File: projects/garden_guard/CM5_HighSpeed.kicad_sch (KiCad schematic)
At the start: 28 parts, among them J1 Conn_02x07_Odd_Even, J2 Conn_01x03, J3 Conn_01x04, J4 Micro_SD_Card_Det, SW1 Tact button, U1 SN74LVC1G07DBVR, U2 TPD4EUSB30, U3 TPD4EUSB30, U4 RT9742GGJ5, U5 MagJack-A70-112-331N126

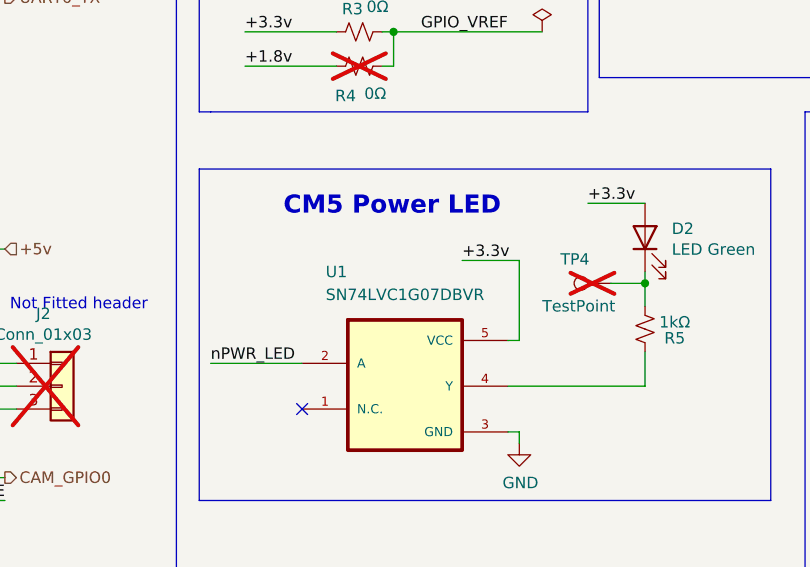
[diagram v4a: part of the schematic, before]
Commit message: - Assign 3D models to lingering footprints lacking them - Start playing with board layout - Move CM5 library files from project to components dir
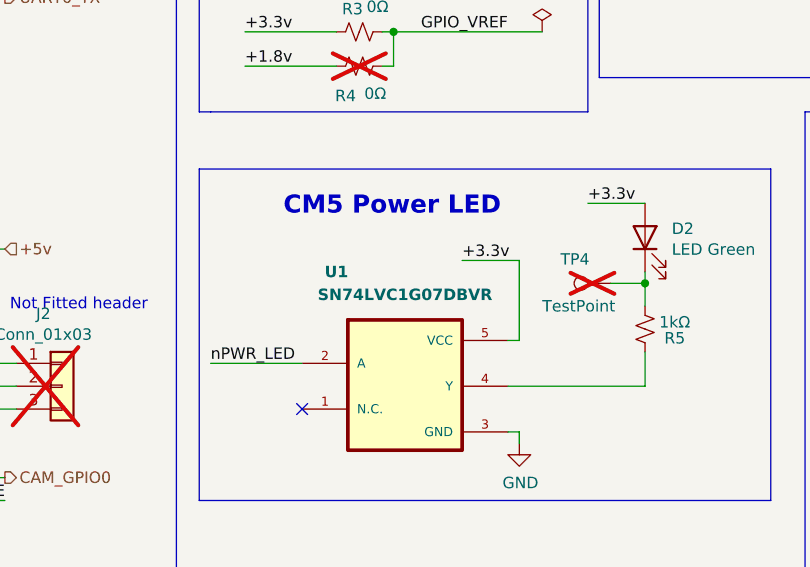
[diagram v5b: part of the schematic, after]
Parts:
- Module1: footprint CM5IO:Raspberry-Pi-5-Compute-Module -> CM5IO:Raspberry-Pi-5-Compute-Module_tall
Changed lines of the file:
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@@
 				(font
 					(size 1.27 1.27)
+					(thickness 0.254)
+					(bold yes)
 				)
 			)
@@
 				(font
 					(size 1.27 1.27)
+					(thickness 0.254)
+					(bold yes)
 				)
 			)
@@
 			)
 		)
-		(property "Footprint" "CM5IO:Raspberry-Pi-5-Compute-Module"
+		(property "Footprint" "CM5IO:Raspberry-Pi-5-Compute-Module_tall"
 			(at 214.63 104.14 0)
 			(effects

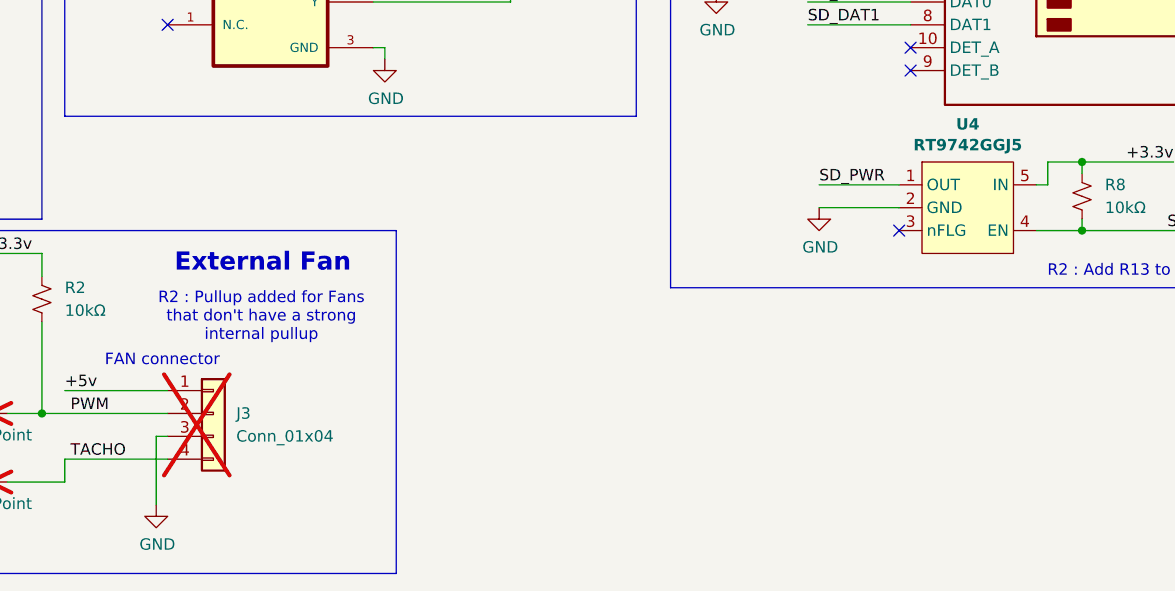
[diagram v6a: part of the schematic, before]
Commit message: - Add M.2 power and connector layout - Add micro HDMI to schematic and layout - Add microSD layout - Add IR illuminator and solenoid output MOSFET layouts - Add USB-C layout
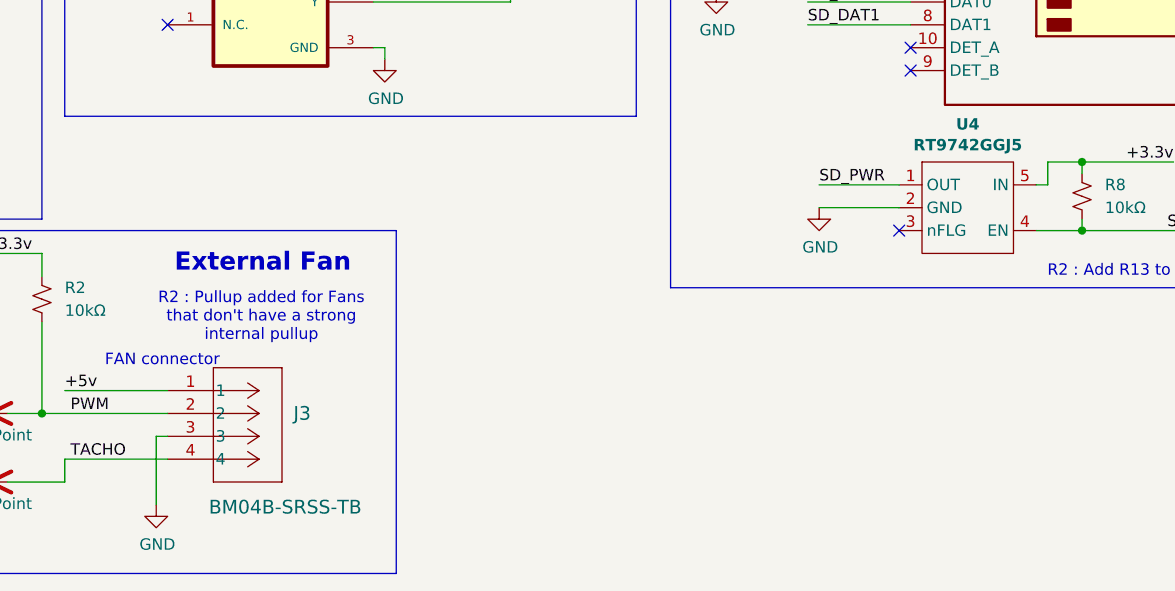
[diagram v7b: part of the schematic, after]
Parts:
- removed J3: Conn_01x04, Connector_PinHeader_2.54mm:PinHeader_1x04_P2.54mm_Vertical, symbol Connector_Generic:Conn_01x04
- added J3: BM04B-SRSS-TB, Custom_Connector:BM04B-SRSS_JST, symbol Custom_Connector:BM04B-SRSS-TB
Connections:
- net +5v: now also J3.1
- net GND: now also J3.3
- net PWM: now also J3.2
- net TACHO: now also J3.4
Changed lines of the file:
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@@
 	)
 	(symbol
+		(lib_name "TPD4EUSB30_1")
 		(lib_id "CM5IO:TPD4EUSB30")
 		(at 207.01 33.02 0)
@@
 	)
 	(symbol
-		(lib_id "Connector_Generic:Conn_01x04")
-		(at 154.94 179.07 0)
+		(lib_id "Custom_Connector:BM04B-SRSS-TB")
+		(at 149.86 176.53 0)
 		(unit 1)
 		(exclude_from_sim no)
-		(in_bom no)
+		(in_bom yes)
 		(on_board yes)
-		(dnp yes)
-		(fields_autoplaced yes)
+		(dnp no)
 		(property "Reference" "J3"
-			(at 157.48 179.0699 0)
-			(effects
-				(font
-					(size 1.27 1.27)
+			(at 163.83 179.0699 0)
+			(effects
+				(font
+					(size 1.524 1.524)
 				)
 				(justify left)
 			)
 		)
-		(property "Value" "Conn_01x04"
-			(at 157.48 181.6099 0)
-			(effects
-				(font
-					(size 1.27 1.27)
+		(property "Value" "BM04B-SRSS-TB"
+			(at 154.432 189.484 0)
+			(effects
+				(font
+					(size 1.524 1.524)
 				)
 				(justify left)
 			)
 		)
-		(property "Footprint" "Connector_PinHeader_2.54mm:PinHeader_1x04_P2.54mm_Vertical"
-			(at 154.94 179.07 0)
-			(effects
-				(font
-					(size 1.27 1.27)
-				)
-				(hide yes)
-			)
-		)
-		(property "Datasheet" "~"
-			(at 154.94 179.07 0)
-			(effects
-				(font
-					(size 1.27 1.27)
-				)
-				(hide yes)
-			)
-		)
-		(property "Description" "Generic connector, single row, 01x04, script generated (kicad-library-utils/schlib/autogen/connector/)"
-			(at 154.94 179.07 0)
-			(effects
-				(font
-					(size 1.27 1.27)
-				)
-				(hide yes)
-			)
+		(property "Footprint" "Custom_Connector:BM04B-SRSS_JST"
+			(at 149.86 191.008 0)
+			(effects
+				(font
+					(size 1.27 1.27)
+					(italic yes)
+				)
+				(hide yes)
+			)
+		)
+		(property "Datasheet" "BM04B-SRSS-TB"
+			(at 149.86 176.53 0)
+			(effects
+				(font
+					(size 1.27 1.27)
+					(italic yes)
+				)
+				(hide yes)
+			)
+		)
+		(property "Description" "JST SH 4-Pin Vertical"
+			(at 149.86 176.53 0)
+			(effects
+				(font
+					(size 1.27 1.27)
+				)
+				(hide yes)
+			)
+		)
+		(pin "2"
 		)
 		(pin "4"
 		)
+		(pin "1"
+		)
 		(pin "3"
 		)
-		(pin "2"
-		)
-		(pin "1"
-		)
 		(instances
-			(project "garden_guard"
+			(project ""
 				(path "/dcdac9d4-ef08-426f-b97c-7b9219501e71/3824b291-1119-4235-959b-f8a35bb4573d"
 					(reference "J3")

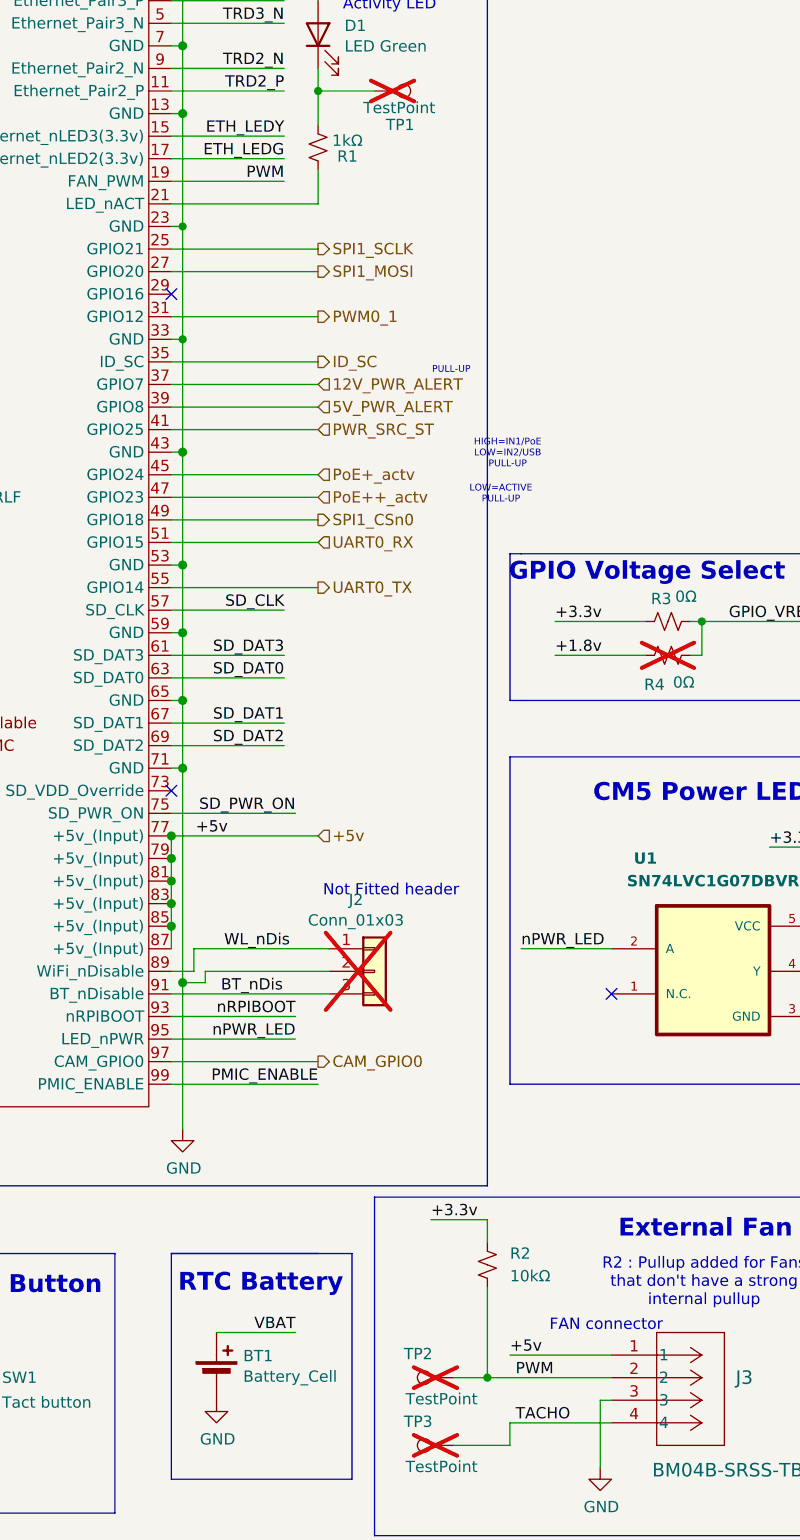
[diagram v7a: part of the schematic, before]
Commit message: - Route Ethernet connector (nearly there) - Update PWM net to FAN_PWM
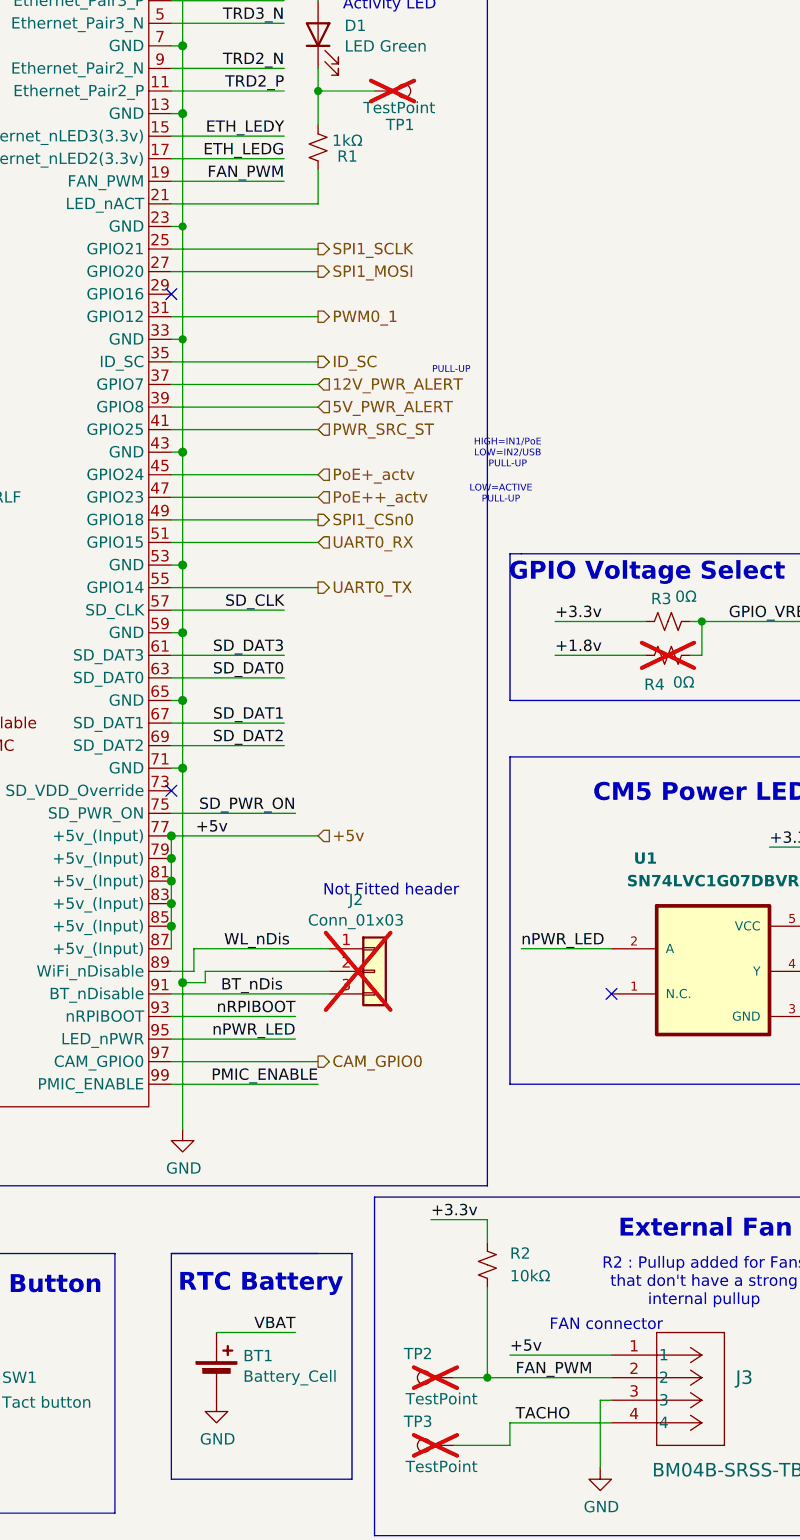
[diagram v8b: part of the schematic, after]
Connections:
- net PWM renamed FAN_PWM
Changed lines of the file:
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@@
 		)
 	)
-	(label "PWM"
+	(label "FAN_PWM"
 		(at 113.03 44.45 180)
 		(effects
@@
 		)
 	)
-	(label "PWM"
+	(label "FAN_PWM"
 		(at 139.065 179.07 0)
 		(effects
